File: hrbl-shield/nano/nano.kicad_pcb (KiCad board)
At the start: 2 copper layers, 17.8 x 43.2 mm, 7 parts, among them P1 Digital, P2 Analog, P3 CONN_01X01, P4 CONN_01X01, P5 CONN_01X01, P6 CONN_01X01

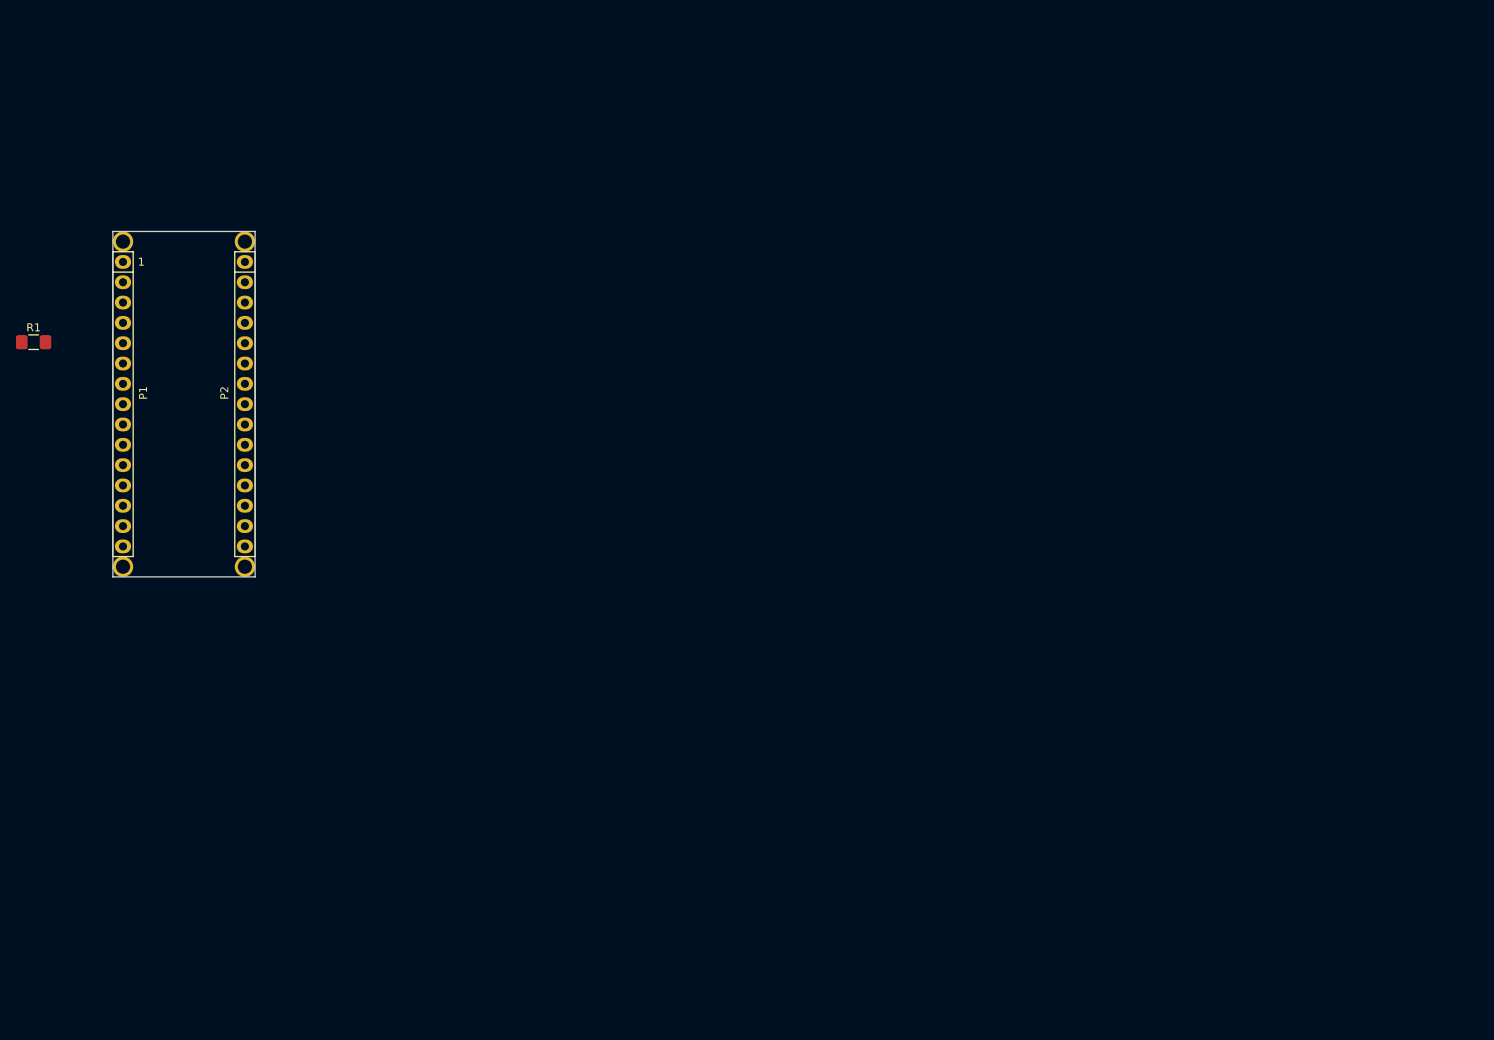
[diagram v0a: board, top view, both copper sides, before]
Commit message: Updated nano card
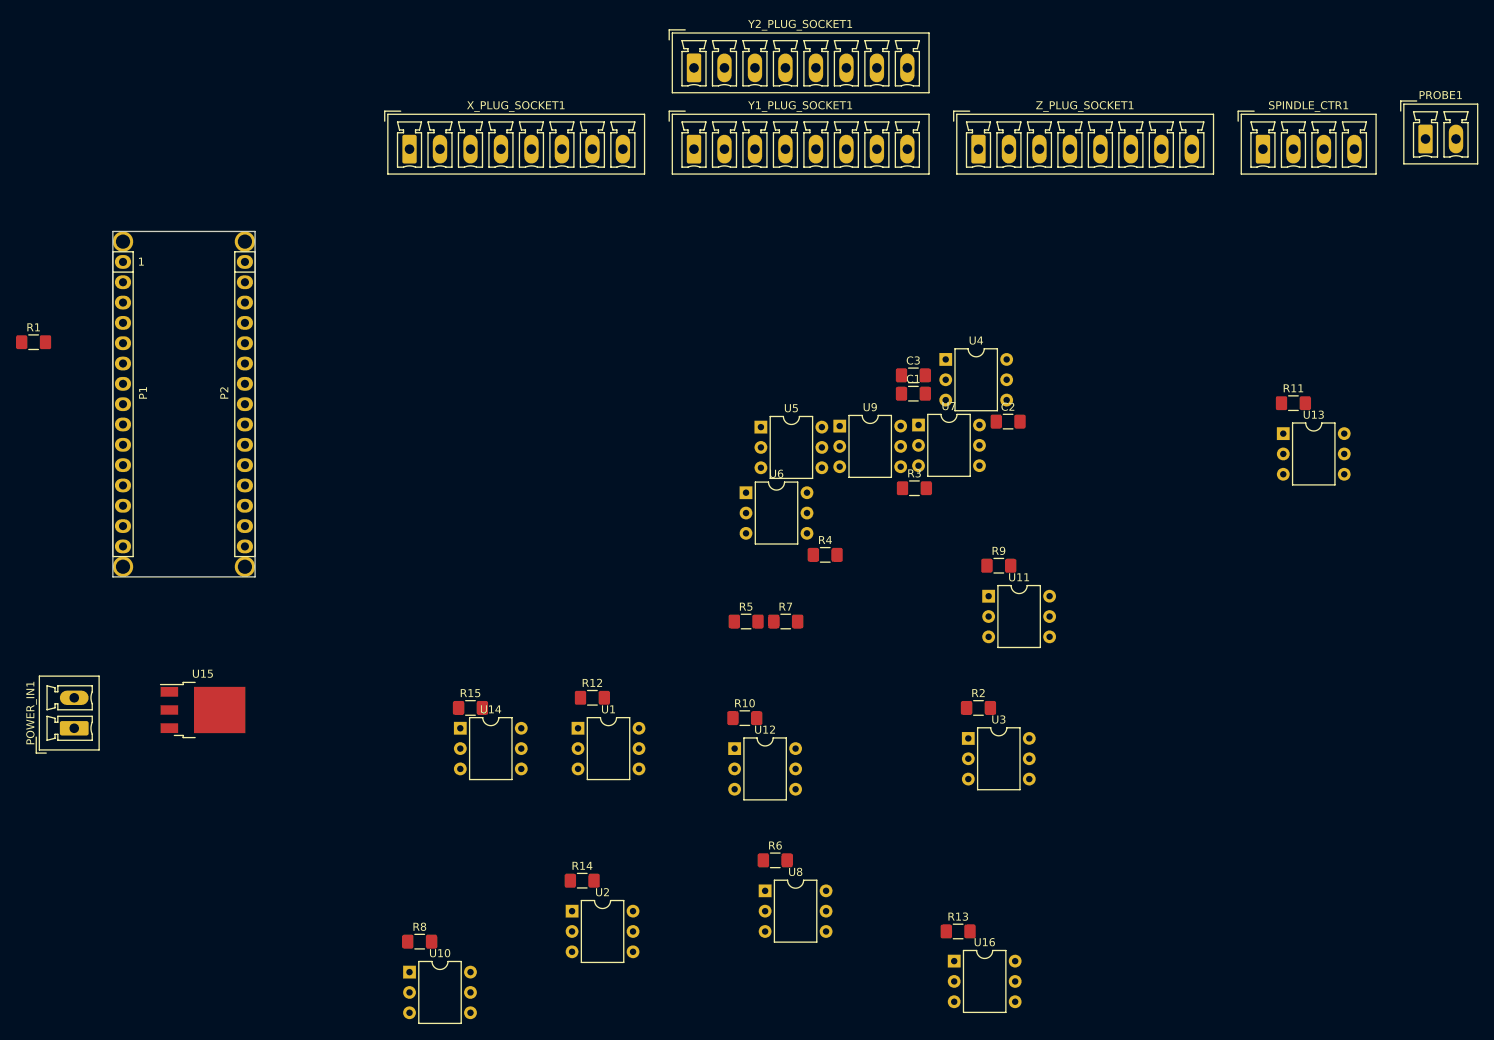
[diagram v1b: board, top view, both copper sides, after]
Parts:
- added C1: 10uF, Capacitor_SMD:C_1206_3216Metric_Pad1.42x1.75mm_HandSolder, F.Cu at (238.2, 87.7)
- added C2: 100nF (0.1uF), Capacitor_SMD:C_1206_3216Metric_Pad1.42x1.75mm_HandSolder, F.Cu at (250.1, 91.2)
- added C3: 100nF (0.1uF), Capacitor_SMD:C_1206_3216Metric_Pad1.42x1.75mm_HandSolder, F.Cu at (238.2, 85.4)
- added POWER_IN1: Conn_01x02, Connector_Phoenix_MC:PhoenixContact_MCV_1,5_2-G-3.81_1x02_P3.81mm_Vertical, F.Cu at (133.3, 129.5)
- added PROBE1: Conn_01x02, Connector_Phoenix_MC:PhoenixContact_MCV_1,5_2-G-3.81_1x02_P3.81mm_Vertical, F.Cu at (302.3, 55.9)
- added R10: 220, Resistor_SMD:R_1206_3216Metric_Pad1.42x1.75mm_HandSolder, F.Cu at (217.2, 128.3)
- added R11: 220, Resistor_SMD:R_1206_3216Metric_Pad1.42x1.75mm_HandSolder, F.Cu at (285.8, 88.9)
- added R12: 220, Resistor_SMD:R_1206_3216Metric_Pad1.42x1.75mm_HandSolder, F.Cu at (198.1, 125.7)
- added R13: 220, Resistor_SMD:R_1206_3216Metric_Pad1.42x1.75mm_HandSolder, F.Cu at (243.8, 154.9)
- added R14: 220, Resistor_SMD:R_1206_3216Metric_Pad1.42x1.75mm_HandSolder, F.Cu at (196.8, 148.6)
- added R15: 220, Resistor_SMD:R_1206_3216Metric_Pad1.42x1.75mm_HandSolder, F.Cu at (182.9, 127.0)
- added R2: 220, Resistor_SMD:R_1206_3216Metric_Pad1.42x1.75mm_HandSolder, F.Cu at (246.4, 127.0)
- added R3: 220, Resistor_SMD:R_1206_3216Metric_Pad1.42x1.75mm_HandSolder, F.Cu at (238.4, 99.5)
- added R4: 220, Resistor_SMD:R_1206_3216Metric_Pad1.42x1.75mm_HandSolder, F.Cu at (227.2, 107.9)
- added R5: 220, Resistor_SMD:R_1206_3216Metric_Pad1.42x1.75mm_HandSolder, F.Cu at (217.3, 116.2)
- added R6: 220, Resistor_SMD:R_1206_3216Metric_Pad1.42x1.75mm_HandSolder, F.Cu at (221.0, 146.1)
- added R7: 220, Resistor_SMD:R_1206_3216Metric_Pad1.42x1.75mm_HandSolder, F.Cu at (222.3, 116.2)
- added R8: 220, Resistor_SMD:R_1206_3216Metric_Pad1.42x1.75mm_HandSolder, F.Cu at (176.5, 156.2)
- added R9: 220, Resistor_SMD:R_1206_3216Metric_Pad1.42x1.75mm_HandSolder, F.Cu at (248.9, 109.2)
- added SPINDLE_CTR1: Conn_01x04, Connector_Phoenix_MC:PhoenixContact_MCV_1,5_4-G-3.81_1x04_P3.81mm_Vertical, F.Cu at (281.9, 57.1)
- added U1: 4N25, Package_DIP:DIP-6_W7.62mm, F.Cu at (196.3, 129.5)
- added U10: 4N25, Package_DIP:DIP-6_W7.62mm, F.Cu at (175.3, 160.0)
- added U11: 4N25, Package_DIP:DIP-6_W7.62mm, F.Cu at (247.7, 113.0)
- added U12: 4N25, Package_DIP:DIP-6_W7.62mm, F.Cu at (215.9, 132.1)
- added U13: 4N25, Package_DIP:DIP-6_W7.62mm, F.Cu at (284.5, 92.7)
- added U14: 4N25, Package_DIP:DIP-6_W7.62mm, F.Cu at (181.6, 129.5)
- added U15: IFX27001TFV50ATMA1CT-ND, Package_TO_SOT_SMD:TO-252-3_TabPin2, F.Cu at (149.4, 127.3)
- added U16: 4N25, Package_DIP:DIP-6_W7.62mm, F.Cu at (243.3, 158.6)
- added U2: 4N25, Package_DIP:DIP-6_W7.62mm, F.Cu at (195.6, 152.4)
- added U3: 4N25, Package_DIP:DIP-6_W7.62mm, F.Cu at (245.1, 130.8)
- added U4: 4N25, Package_DIP:DIP-6_W7.62mm, F.Cu at (242.3, 83.4)
- added U5: 4N25, Package_DIP:DIP-6_W7.62mm, F.Cu at (219.2, 91.9)
- added U6: 4N25, Package_DIP:DIP-6_W7.62mm, F.Cu at (217.3, 100.1)
- added U7: 4N25, Package_DIP:DIP-6_W7.62mm, F.Cu at (238.9, 91.6)
- added U8: 4N25, Package_DIP:DIP-6_W7.62mm, F.Cu at (219.7, 149.9)
- added U9: 4N25, Package_DIP:DIP-6_W7.62mm, F.Cu at (229.0, 91.8)
- added X_PLUG_SOCKET1: Conn_01x08, Connector_Phoenix_MC:PhoenixContact_MCV_1,5_8-G-3.81_1x08_P3.81mm_Vertical, F.Cu at (175.3, 57.1)
- added Y1_PLUG_SOCKET1: Conn_01x08, Connector_Phoenix_MC:PhoenixContact_MCV_1,5_8-G-3.81_1x08_P3.81mm_Vertical, F.Cu at (210.8, 57.1)
- added Y2_PLUG_SOCKET1: Conn_01x08, Connector_Phoenix_MC:PhoenixContact_MCV_1,5_8-G-3.81_1x08_P3.81mm_Vertical, F.Cu at (210.8, 47.0)
- added Z_PLUG_SOCKET1: Conn_01x08, Connector_Phoenix_MC:PhoenixContact_MCV_1,5_8-G-3.81_1x08_P3.81mm_Vertical, F.Cu at (246.4, 57.1)
- R1: value R -> 220
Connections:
- P1 pad 10: (no net) -> DIR_Z
- P1 pad 12: (no net) -> LIM_X
- P1 pad 13: (no net) -> LIM_Y
- P1 pad 14: (no net) -> SPINDLE_PWM
- P1 pad 15: (no net) -> LIM_Z
- P1 pad 6: (no net) -> PUL_Y
- P1 pad 7: (no net) -> PUL_Z
- P1 pad 8: (no net) -> DIR_X
- P1 pad 9: (no net) -> DIR_Y
- P2 pad 12: (no net) -> ABORT
- P2 pad 15: (no net) -> SPINDLE_EN
- P2 pad 4: (no net) -> +5V
- P2 pad 7: (no net) -> PROBE
- R1 pad 1: PUL_X -> Net-(R1-Pad1)
- R1 pad 2: (no net) -> PUL_X

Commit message: Updated nano card
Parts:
- C1, C2, C3, R1, R10, R11, R12, R13, R14, R15, R2, R3, R4, R5, R6, R7, R8, R9, U15: moved to B.Cu
- U1, U10, U11, U12, U13, U14, U16, U2, U3, U4, U5, U6, U7, U8, U9: value 4N25 -> SFH6206-3T; footprint Package_DIP:DIP-6_W7.62mm -> Package_DIP:SMDIP-4_W9.53mm_Clearance8mm; moved to B.Cu
- moved PROBE1 244.1 mm to (70.8, 133.4), turned to 270 degrees
- moved SPINDLE_CTR1 228.6 mm to (70.8, 144.8), turned to 270 degrees
- moved Z_PLUG_SOCKET1 180.5 mm to (70.8, 99.1), turned to 270 degrees
- moved R11 159.2 mm to (129.3, 118.4)
- moved Y1_PLUG_SOCKET1 150.3 mm to (60.6, 63.6), turned to 270 degrees
- moved Y2_PLUG_SOCKET1 141.0 mm to (70.8, 63.6), turned to 270 degrees
- moved C2 139.6 mm to (114.9, 56.1), turned to 270 degrees
- moved R2 133.8 mm to (114.0, 107.2)
- moved U11 128.7 mm to (120.4, 93.3), turned to 180 degrees
- moved POWER_IN1 126.8 mm to (70.6, 19.3), turned to 270 degrees
- moved R3 125.4 mm to (114.0, 115.8)
- moved U4 123.4 mm to (120.4, 103.2)
- moved U8 122.5 mm to (120.4, 78.1), turned to 180 degrees
- moved U7 121.7 mm to (120.4, 119.7), turned to 180 degrees
- moved C1 120.7 mm to (120.5, 61.1), turned to 180 degrees
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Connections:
- PROBE1 pad 2: Net-(PROBE1-Pad2) -> /PROBE_PLATE
- R15 pad 1: Net-(R15-Pad1) -> /PWR_SIG
- U1 pad 3: (no net) -> GNDPWR
- U1 pad 4: GNDPWR -> /PWR_SIG
- U10 pad 1: Net-(R8-Pad1) -> Net-(R7-Pad1)
- U10 pad 3: (no net) -> DIR_X_OUT
- U10 pad 4: DIR_Y_OUT -> 5V_ISO
- U11 pad 1: Net-(R9-Pad1) -> Net-(R8-Pad1)
- U11 pad 3: (no net) -> DIR_Y_OUT
- U11 pad 4: DIR_Z_OUT -> 5V_ISO
- U12 pad 1: Net-(R10-Pad1) -> Net-(R9-Pad1)
- U12 pad 3: (no net) -> DIR_Z_OUT
- U12 pad 4: /SPINDLE_EN_OUT -> 5V_ISO
- U13 pad 1: Net-(R11-Pad1) -> Net-(R10-Pad1)
- U13 pad 3: (no net) -> /SPINDLE_EN_OUT
- U13 pad 4: /SPINDLE_PWM_OUT -> /+24V_IN
- U14 pad 1: Net-(R15-Pad1) -> Net-(R4-Pad1)
- U14 pad 2: GNDPWR -> LIM_Z_IN
- U14 pad 3: (no net) -> GND
- U14 pad 4: GND -> LIM_Z
- U16 pad 1: Net-(R13-Pad1) -> Net-(R14-Pad1)
- U16 pad 2: ALARM_IN -> /PROBE_PLATE
- U16 pad 3: (no net) -> GND
- U16 pad 4: GND -> PROBE
- U2 pad 1: Net-(R14-Pad1) -> /PWR_SIG
- U2 pad 2: Net-(PROBE1-Pad2) -> GNDPWR
- U2 pad 3: (no net) -> GND
- U2 pad 4: GND -> ABORT
- U3 pad 1: Net-(R2-Pad1) -> Net-(R13-Pad1)
- U3 pad 2: LIM_X_IN -> ALARM_IN
- U3 pad 3: (no net) -> GND
- U3 pad 4: GND -> ABORT
- U4 pad 1: Net-(R3-Pad1) -> Net-(R2-Pad1)
- U4 pad 2: LIM_Y_IN -> LIM_X_IN
- U4 pad 3: (no net) -> GND
- U4 pad 4: GND -> LIM_X
- U5 pad 1: Net-(R4-Pad1) -> Net-(R3-Pad1)
- U5 pad 2: LIM_Z_IN -> LIM_Y_IN
- U5 pad 3: (no net) -> GND
- U5 pad 4: GND -> LIM_Y
- U6 pad 3: (no net) -> PUL_X_OUT
- U6 pad 4: PUL_X_OUT -> 5V_ISO
- U7 pad 1: Net-(R5-Pad1) -> Net-(R11-Pad1)
- U7 pad 3: (no net) -> /SPINDLE_PWM_OUT
- U7 pad 4: PUL_Y_OUT -> 5V_ISO
- U8 pad 1: Net-(R6-Pad1) -> Net-(R5-Pad1)
- U8 pad 3: (no net) -> PUL_Y_OUT
- U8 pad 4: PUL_Z_OUT -> 5V_ISO
- U9 pad 1: Net-(R7-Pad1) -> Net-(R6-Pad1)
- U9 pad 3: (no net) -> PUL_Z_OUT
- U9 pad 4: DIR_X_OUT -> 5V_ISO
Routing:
- net 5V_ISO: track 0.00 -> 168.4 mm
- net GND: track 0.00 -> 142.1 mm
- net GNDPWR: track 0.00 -> 126.8 mm
- net LIM_Z: track 0.00 -> 25.9 mm
- net LIM_Y: track 0.00 -> 19.0 mm
- net SPINDLE_PWM: track 0.00 -> 18.5 mm
- net ABORT: track 0.00 -> 17.6 mm
- net LIM_X: track 0.00 -> 16.4 mm
- net /PWR_SIG: track 0.00 -> 15.5 mm
- net Net-(R1-Pad1): track 0.00 -> 14.2 mm
- net Net-(R5-Pad1): track 0.00 -> 11.5 mm
- net Net-(R6-Pad1): track 0.00 -> 10.4 mm
- net Net-(R9-Pad1): track 0.00 -> 9.47 mm
- net Net-(R7-Pad1): track 0.00 -> 9.39 mm
- net PROBE: track 0.00 -> 8.87 mm
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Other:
- board size 17.8 x 43.2 mm -> 148.3 x 158 mm
- net class Default: clearance 0.2 -> 0.45; trace_width 0.25 -> 0.35
- rule trace_clearance: 0.2 -> 0.45

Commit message: Updated nano sheild
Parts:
- added R16: 0, Resistor_SMD:R_1206_3216Metric_Pad1.42x1.75mm_HandSolder, B.Cu at (85.7, 60.8)
- added R17: 0, Resistor_SMD:R_1206_3216Metric_Pad1.42x1.75mm_HandSolder, B.Cu at (85.7, 93.6)
- added R18: 0, Resistor_SMD:R_1206_3216Metric_Pad1.42x1.75mm_HandSolder, B.Cu at (85.9, 126.5)
- added R19: 0, Resistor_SMD:R_1206_3216Metric_Pad1.42x1.75mm_HandSolder, B.Cu at (112.6, 85.6)
- moved Y2_PLUG_SOCKET1 38.6 mm to (106.4, 78.4)
- moved PROBE1 37.4 mm to (91.7, 164.5)
- moved Y1_PLUG_SOCKET1 34.5 mm to (91.7, 78.4)
- moved X_PLUG_SOCKET1 27.2 mm to (91.8, 45.2)
- moved POWER_IN1 26.5 mm to (91.8, 35.2)
- moved Z_PLUG_SOCKET1 24.2 mm to (91.6, 111.5)
- moved SPINDLE_CTR1 20.9 mm to (91.7, 144.5)
- moved R10 3.78 mm to (157.5, 112.1)
- moved U13 3.23 mm to (164.1, 106.8)
- moved R4 3.18 mm to (117.2, 129.2)
- moved R13 2.42 mm to (174.1, 87.5)
- moved R12 2.37 mm to (174.1, 98.7)
- moved U1 2.37 mm to (164.1, 99.9)
- moved R15 2.29 mm to (174.1, 92.7)
- moved U3 2.29 mm to (164.1, 88.8)
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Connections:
- U9 pad 3: PUL_Z_OUT -> Net-(R19-Pad2)
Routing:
- net GNDPWR: track 126.8 -> 558.0 mm, vias 0 -> 4
- net ALARM_IN: track 0.00 -> 260.0 mm
- net +36V: track 3.24 -> 184.9 mm, vias 0 -> 4
- net LIM_X_IN: track 0.00 -> 134.9 mm, vias 0 -> 2
- net /PROBE_PLATE: track 0.00 -> 134.7 mm
- net /+24V_IN: track 0.00 -> 122.6 mm
- net /SPINDLE_EN_OUT: track 0.00 -> 118.3 mm
- net PUL_Z_OUT: track 0.00 -> 91.6 mm
- net DIR_X_OUT: track 0.00 -> 74.5 mm
- net /SPINDLE_PWM_OUT: track 0.00 -> 47.2 mm
- net DIR_Z_OUT: track 0.00 -> 46.5 mm
- net PUL_X_OUT: track 0.00 -> 39.5 mm
- net LIM_Z_IN: track 0.00 -> 29.9 mm
- net DIR_Y_OUT: track 0.00 -> 29.4 mm
- net LIM_Y_IN: track 0.00 -> 26.9 mm
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- added copper zone on B.Cu, net 5V_ISO
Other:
- net class Default: via_dia 0.6 -> 1.5; via_drill 0.4 -> 1
- net class Power added: clearance 0.45, trace_width 1.5, via_dia 2, via_drill 1
- rule trace_min: 0.2 -> 0.35
- rule via_min_size: 0.4 -> 1

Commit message: updated Nano shield
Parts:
- added R20: 0, Resistor_SMD:R_1206_3216Metric_Pad1.42x1.75mm_HandSolder, B.Cu at (116.3, 60.8)
- moved C1 4.81 mm to (116.3, 63.5)
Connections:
- C1 pad 2: GNDPWR -> GNDS
- PROBE1 pad 1: GNDPWR -> GNDS
- SPINDLE_CTR1 pad 3: GNDPWR -> GNDS
- U1 pad 2: GNDPWR -> GNDS
- U1 pad 3: GNDPWR -> GNDS
- U2 pad 2: GNDPWR -> GNDS
- X_PLUG_SOCKET1 pad 2: GNDPWR -> GNDS
- X_PLUG_SOCKET1 pad 4: GNDPWR -> GNDS
- Y1_PLUG_SOCKET1 pad 2: GNDPWR -> GNDS
- Y1_PLUG_SOCKET1 pad 4: GNDPWR -> GNDS
- Y2_PLUG_SOCKET1 pad 2: GNDPWR -> GNDS
- Y2_PLUG_SOCKET1 pad 4: GNDPWR -> GNDS
- Z_PLUG_SOCKET1 pad 2: GNDPWR -> GNDS
- Z_PLUG_SOCKET1 pad 4: GNDPWR -> GNDS
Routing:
- net GNDPWR: track 558.0 -> 176.5 mm
- net GNDS: track 0.00 -> 380.1 mm
- net 5V_ISO: track 174.2 -> 180.5 mm
- net +36V: track 184.9 -> 190.9 mm
- net LIM_X_IN: track 134.9 -> 129.0 mm
- net PUL_Y_OUT: track 24.4 -> 29.8 mm
- net /+24V_IN: track 122.6 -> 119.3 mm
- net LIM_Y_IN: track 26.9 -> 29.0 mm
- net DIR_X_OUT: track 74.5 -> 76.3 mm
- net DIR_Z_OUT: track 46.5 -> 48.2 mm
- net PUL_Z_OUT: track 91.6 -> 92.8 mm
- net LIM_Z: track 25.9 -> 27.0 mm
- net /SPINDLE_EN_OUT: track 118.3 -> 117.6 mm
- net ALARM_IN: track 260.0 -> 260.5 mm
- added copper zone on B.Cu, net +36V
- added copper zone on F.Cu, net +36V
- added copper zone on B.Cu, net GND
- added copper zone on B.Cu, net GNDPWR
- added copper zone on F.Cu, net GNDPWR
- added copper zone on B.Cu, net GNDS
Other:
- board size 148.3 x 158 mm -> 96.8 x 140.1 mm

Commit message: Updated board
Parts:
- moved U6 3.94 mm to (120.4, 69.0)
- moved U8 3.43 mm to (120.4, 74.7)
- moved U9 2.79 mm to (120.4, 80.4)
- moved U10 2.16 mm to (120.4, 86.1)
- moved U11 1.52 mm to (120.4, 91.8)
- moved R13 1.02 mm to (174.0, 86.5)
- moved R14 1.02 mm to (174.0, 81.3)
- moved U16 1.02 mm to (164.1, 82.5)
- moved U12 0.89 mm to (120.4, 97.5)
- moved R4 0.76 mm to (117.2, 129.9)
- moved U14 0.76 mm to (120.4, 125.6)
- moved R5 0.54 mm to (134.7, 83.9)
- moved R6 0.54 mm to (134.7, 86.5)
- moved R7 0.54 mm to (134.7, 89.0)
- moved R8 0.54 mm to (134.7, 91.6)
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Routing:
- net /PROBE_PLATE: track 134.7 -> 142.9 mm
- net GND: track 144.6 -> 151.5 mm
- net LIM_Y_IN: track 29.0 -> 35.0 mm
- net PUL_X_OUT: track 39.5 -> 35.5 mm
- net 5V_ISO: track 180.5 -> 184.5 mm
- net Net-(R5-Pad1): track 11.5 -> 15.0 mm
- net Net-(R1-Pad1): track 14.2 -> 17.6 mm
- net GNDS: track 380.1 -> 377.7 mm
- net PUL_Y_OUT: track 29.8 -> 28.2 mm
- net ABORT: track 17.7 -> 19.2 mm
- net DIR_Y_OUT: track 29.4 -> 27.8 mm
- net Net-(R19-Pad2): track 3.15 -> 4.53 mm
- net Net-(R6-Pad1): track 10.4 -> 11.4 mm
- net PROBE: track 6.98 -> 7.94 mm
- net LIM_Z: track 27.0 -> 27.6 mm
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
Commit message: Nano sheild
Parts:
- added MH1: MountingHole, MountingHole:MountingHole_4.5mm_Pad, F.Cu at (154.6, 40.1)
- added MH2: MountingHole, MountingHole:MountingHole_4.5mm_Pad, F.Cu at (119.5, 40.1)
- added MH3: MountingHole, MountingHole:MountingHole_4.5mm_Pad, F.Cu at (154.4, 145.3)
- added MH4: MountingHole, MountingHole:MountingHole_4.5mm_Pad, F.Cu at (119.4, 145.3)
- moved POWER_IN1 0.25 mm to (91.6, 35.2)
- moved X_PLUG_SOCKET1 0.25 mm to (91.6, 45.2)
- moved Y1_PLUG_SOCKET1 0.17 mm to (91.6, 78.4)
- moved PROBE1 0.13 mm to (91.6, 164.5)
- moved SPINDLE_CTR1 0.13 mm to (91.6, 144.5)
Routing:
- net DIR_X_OUT: track 76.5 -> 79.1 mm
- net DIR_Z_OUT: track 48.2 -> 49.5 mm
- net DIR_Y_OUT: track 27.8 -> 28.8 mm
- net GND: track 151.5 -> 152.1 mm
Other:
- outline, holes or cut-outs redrawn
